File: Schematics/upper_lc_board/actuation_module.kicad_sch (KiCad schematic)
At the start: 6 parts

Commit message: final upper control board
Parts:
- R15, R16: footprint Resistor_SMD:R_1206_3216Metric_Pad1.30x1.75mm_HandSolder -> Resistor_SMD:R_0603_1608Metric; Digikey 311-12.1KFRCT-ND -> (none); LCSC C17912 -> C22790
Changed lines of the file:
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@@
 			)
 		)
-		(property "Footprint" "Resistor_SMD:R_1206_3216Metric_Pad1.30x1.75mm_HandSolder"
+		(property "Footprint" "Resistor_SMD:R_0603_1608Metric"
 			(at 107.95 80.518 90)
 			(effects
@@
 			)
 		)
-		(property "Digikey" "311-12.1KFRCT-ND"
+		(property "Digikey" ""
 			(at 107.95 78.74 90)
 			(effects
@@
 			)
 		)
-		(property "LCSC" "C17912"
+		(property "LCSC" "C22790"
 			(at 107.95 78.74 0)
 			(effects
@@
 			)
 		)
-		(property "Footprint" "Resistor_SMD:R_1206_3216Metric_Pad1.30x1.75mm_HandSolder"
+		(property "Footprint" "Resistor_SMD:R_0603_1608Metric"
 			(at 107.95 65.278 90)
 			(effects
@@
 			)
 		)
-		(property "Digikey" "311-12.1KFRCT-ND"
+		(property "Digikey" ""
 			(at 107.95 63.5 90)
 			(effects
@@
 			)
 		)
-		(property "LCSC" "C17912"
+		(property "LCSC" "C22790"
 			(at 107.95 63.5 0)
 			(effects
@@
 		)
 		(instances
-			(project "upper_lc_board_v2"
+			(project "upper_lc_board"
 				(path "/8de962ac-ee95-4233-a205-efbcd04063bc/bb8d84b9-ecb3-4da4-948c-d0cf2dc1ed2d"
 					(page "6")
@@
 		)
 		(instances
-			(project "upper_lc_board_v2"
+			(project "upper_lc_board"
 				(path "/8de962ac-ee95-4233-a205-efbcd04063bc/bb8d84b9-ecb3-4da4-948c-d0cf2dc1ed2d"
 					(page "7")

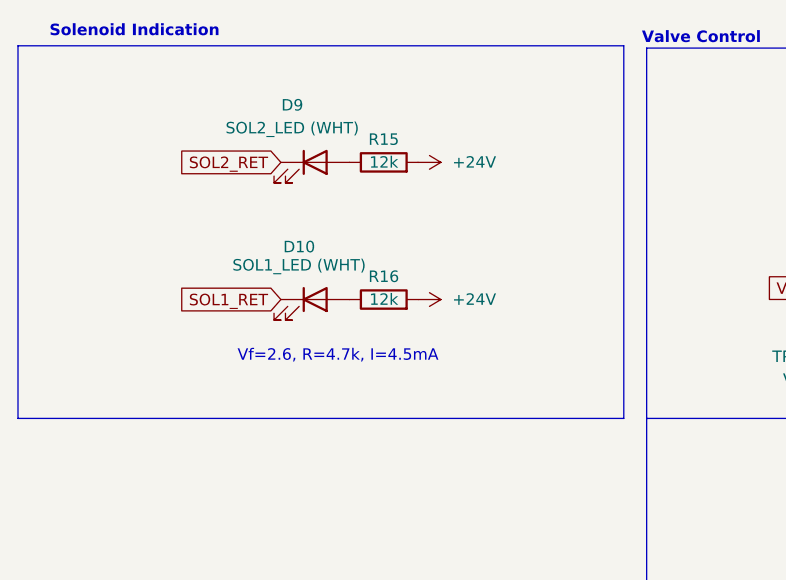
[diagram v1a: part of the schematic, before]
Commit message: added 24V sensing to upper board
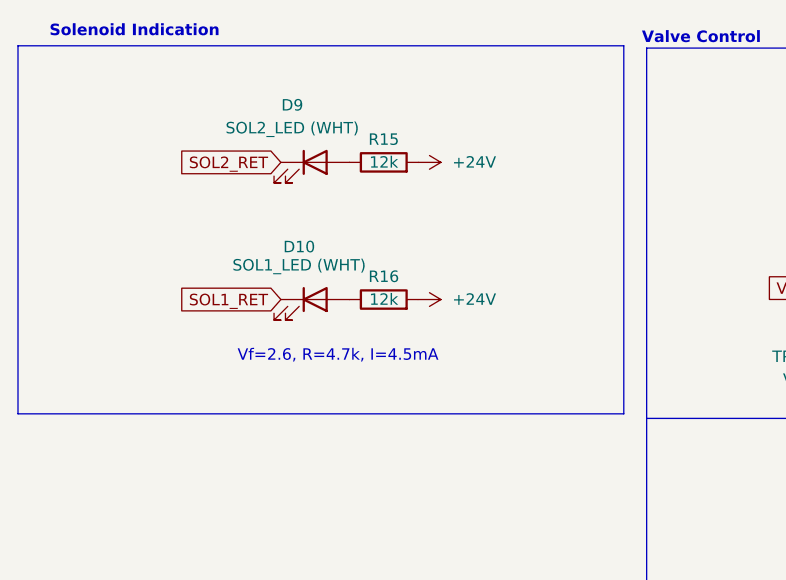
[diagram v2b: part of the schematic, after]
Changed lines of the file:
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@@
 	(rectangle
 		(start 67.31 50.546)
-		(end 134.62 91.948)
+		(end 134.62 91.44)
 		(stroke
 			(width 0)

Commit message: add board-specifc READMEs (TODO), cleanup schematic titles
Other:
- title: Pegasus Solenoid Driver Circuitry -> Solenoid Driver Circuitry
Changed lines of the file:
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@@
 	(paper "A4")
 	(title_block
-		(title "Pegasus Solenoid Driver Circuitry")
+		(title "Solenoid Driver Circuitry")
 		(company "Queen's Rocket Engineering Team")
-		(comment 1 "Upper Control Board V2")
-		(comment 2 "Jeevan Sanchez")
+		(comment 1 "Contributors: Jeevan Sanchez, Tristan Alderson")
+		(comment 2 "PEGASUS - Upper Control Board")
 	)
 	(wire

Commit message: add ed pinouts
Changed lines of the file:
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@@
 		)
 	)
-	(global_label "VALVE1_CTRL"
+	(global_label "SOL1_EN"
 		(shape input)
 		(at 165.1 77.47 180)
@@
 		)
 		(property "Intersheetrefs" "${INTERSHEET_REFS}"
-			(at 149.9591 77.47 0)
+			(at 153.8901 77.47 0)
 			(effects
 				(font
@@
 		)
 	)
-	(global_label "VALVE2_CTRL"
+	(global_label "SOL2_EN"
 		(shape input)
 		(at 162.56 123.19 180)
@@
 		)
 		(property "Intersheetrefs" "${INTERSHEET_REFS}"
-			(at 147.4191 123.19 0)
+			(at 151.3501 123.19 0)
 			(effects
 				(font
